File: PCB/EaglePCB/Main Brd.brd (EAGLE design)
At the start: 110.5 x 90.2 mm, 65 parts, among them J1 1909763-1, J2 702461401, J3 1909763-1, U1 ATWINC1500-MR210PB1952-T, U3 MSP430FR2355TDBTRDBT0038A_M, U6 ARJM11C7-114-BA-EW2

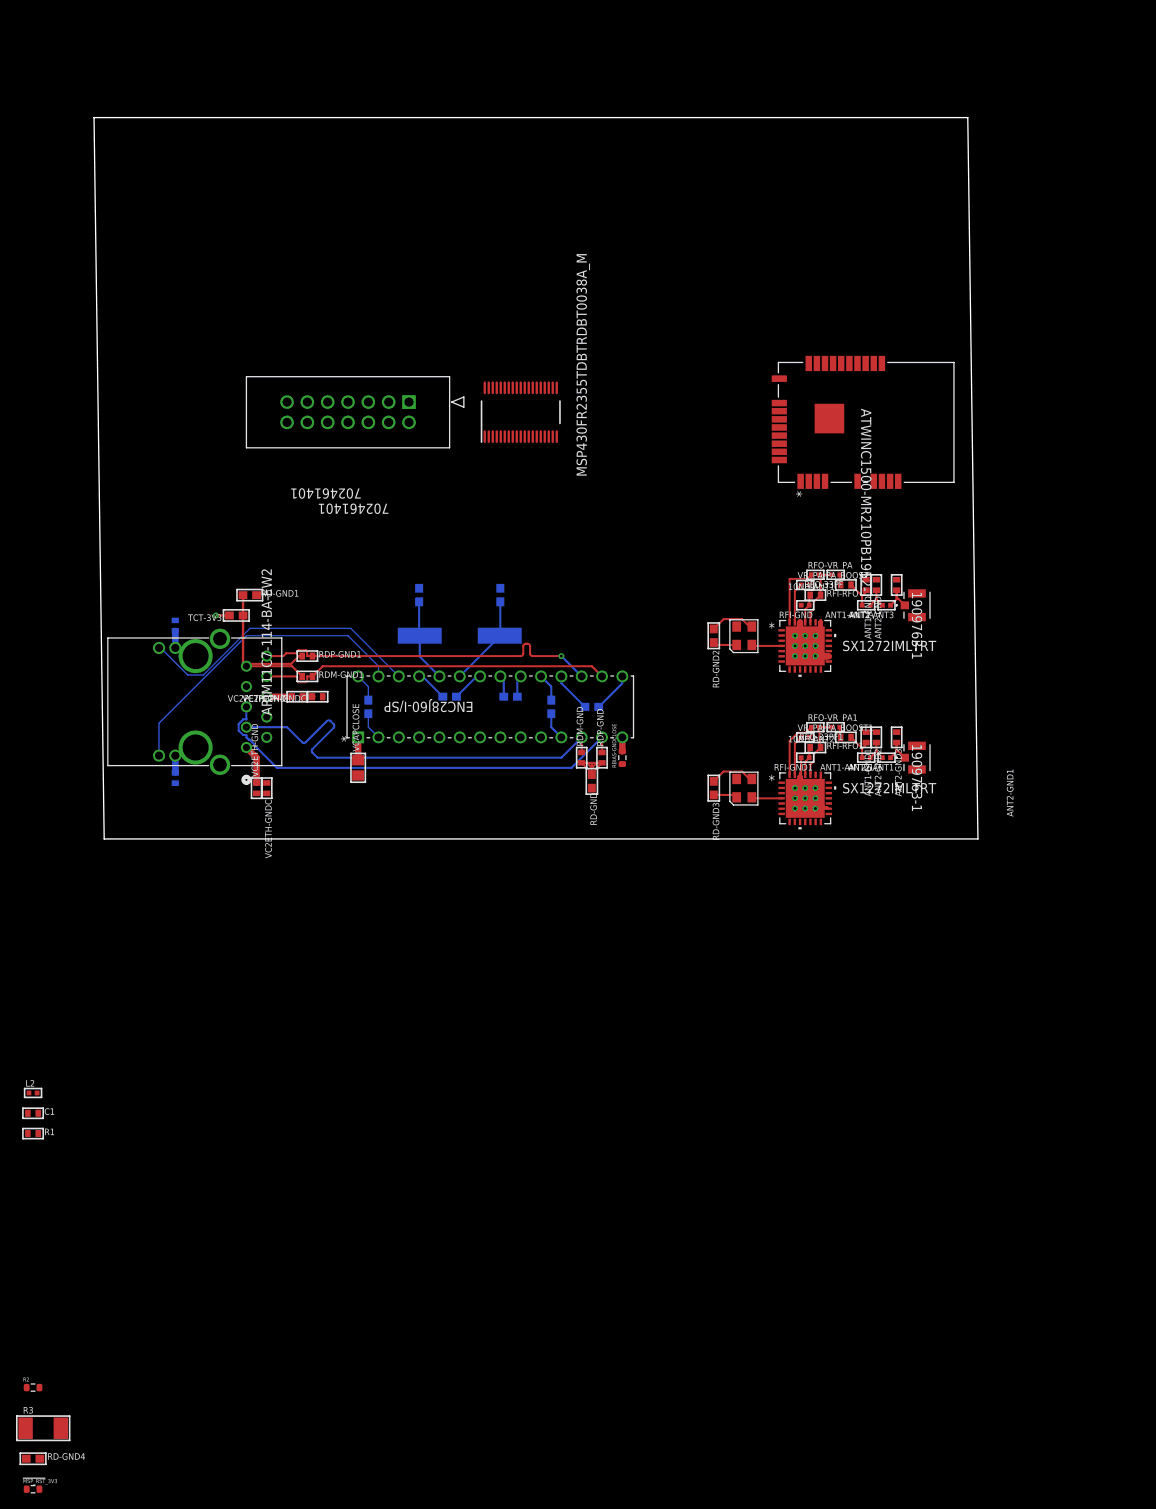
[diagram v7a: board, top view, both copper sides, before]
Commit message: New antenna connector, routing SPI lines
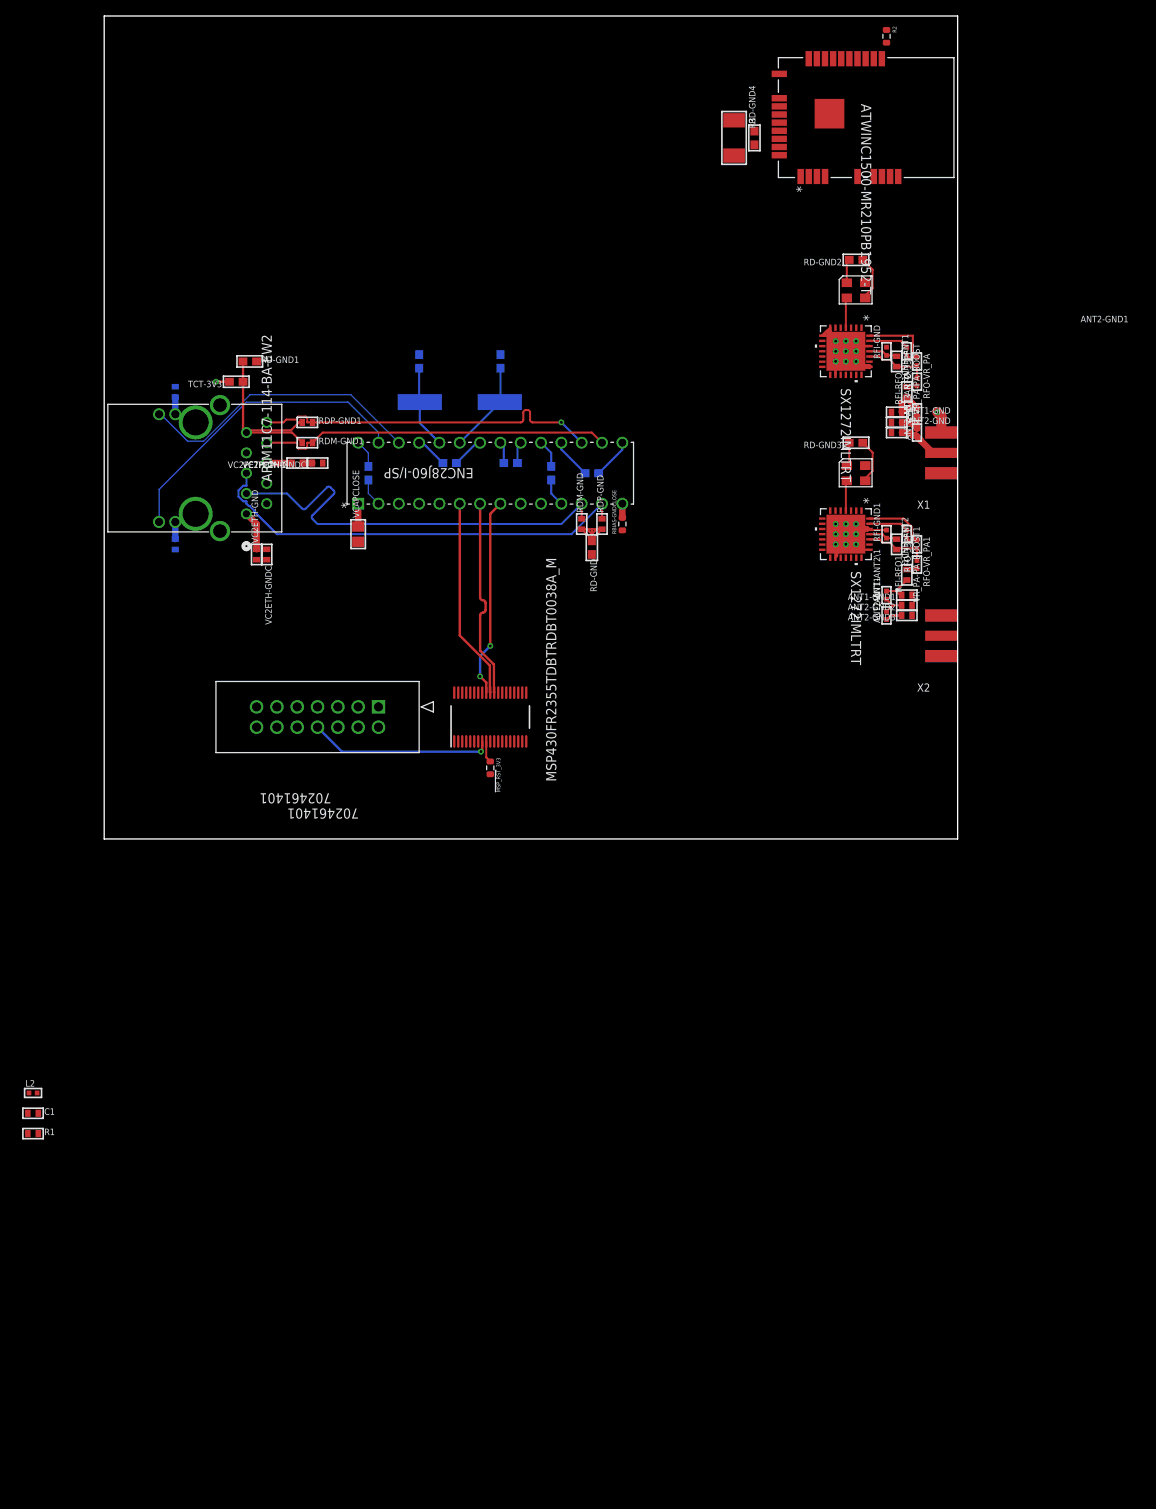
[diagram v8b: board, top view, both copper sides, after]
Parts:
- removed J1, J3: 1909763-1, 473:CONN3_1909763_TEC
- added X1, X2: (no value), adafruit:SMA_EDGELAUNCH
- moved R2 199.8 mm to (97.8, 100.3), turned to 270 degrees
- moved RD-GND4 188.1 mm to (81.3, 87.6), turned to 90 degrees
- moved R3 183.0 mm to (78.7, 87.6), turned to 270 degrees
- moved !MSP_RST!_3V3 106.8 mm to (48.3, 8.89), turned to 270 degrees
- moved RD-GND2 50.2 mm to (94.0, 72.4), turned to 180 degrees
- moved RD-GND3 46.7 mm to (94.0, 49.5), turned to 180 degrees
- moved TCXO1 45.4 mm to (94.0, 68.6), turned to 0 degrees
- moved TCXO2 41.8 mm to (94.0, 45.7), turned to 0 degrees
- moved U3 38.3 mm to (48.3, 15.2)
- moved J2 38.3 mm to (34.3, 16.5)
- moved U1 38.1 mm to (95.2, 90.2)
- moved LORA1 37.2 mm to (92.7, 61.0), turned to 270 degrees
- moved LORA2 33.4 mm to (92.7, 38.1), turned to 270 degrees
- moved RFI-GND 33.3 mm to (97.8, 61.0), turned to 90 degrees
- moved VR_PA-PA_BOOST 31.9 mm to (100.3, 61.0), turned to 270 degrees
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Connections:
- removed net ANT3: ANT2-ANT3.1, ANT2-GND1.2, J1.1
- removed net ANT3-2: ANT2-ANT1.1, ANT2-GND3.2, J3.1
- new net N$11: ANT2-ANT3.1, ANT2-GND1.2, X1.P
- new net N$18: ANT2-ANT1.1, ANT2-GND3.2, X2.P
- net A0_CLK: no longer U3.30
- net A0_MISO: no longer U3.29
- net A0_MOSI: no longer U3.28
- net ETH_MISO: now also U3.29
- net ETH_MOSI: now also U3.28
- net ETH_SCK: now also U3.30
- net GND: now also X1.GND@1, X1.GND@2, X1.GND@3, X1.GND@4, X2.GND@1, X2.GND@2, X2.GND@3, X2.GND@4; no longer J1.2, J1.3, J3.2, J3.3
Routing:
- net ETH_MISO: track 0.00 -> 25.2 mm
- net ETH_SCK: track 0.00 -> 25.0 mm, vias 0 -> 2
- net ETH_MOSI: track 0.00 -> 24.9 mm
- net MSP_TEST: track 0.00 -> 23.0 mm, vias 0 -> 1
- net GND: track 73.9 -> 82.0 mm, vias 16 -> 17
- net N$11: track 0.00 -> 5.50 mm
- net ANT3-2: track 4.52 -> 0.00 mm
- net ANT3: track 4.52 -> 0.00 mm
- net N$18: track 0.00 -> 2.97 mm
- net !MSP_RST: track 0.00 -> 2.71 mm
- net ANT1: track 4.05 -> 6.04 mm
- net ANT2: track 3.28 -> 4.81 mm
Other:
- board size 110.5 x 90.2 mm -> 106.7 x 102.9 mm
